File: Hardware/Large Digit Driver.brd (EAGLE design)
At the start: 45.7 x 22.9 mm, 28 parts, among them U1 TPIC6C596

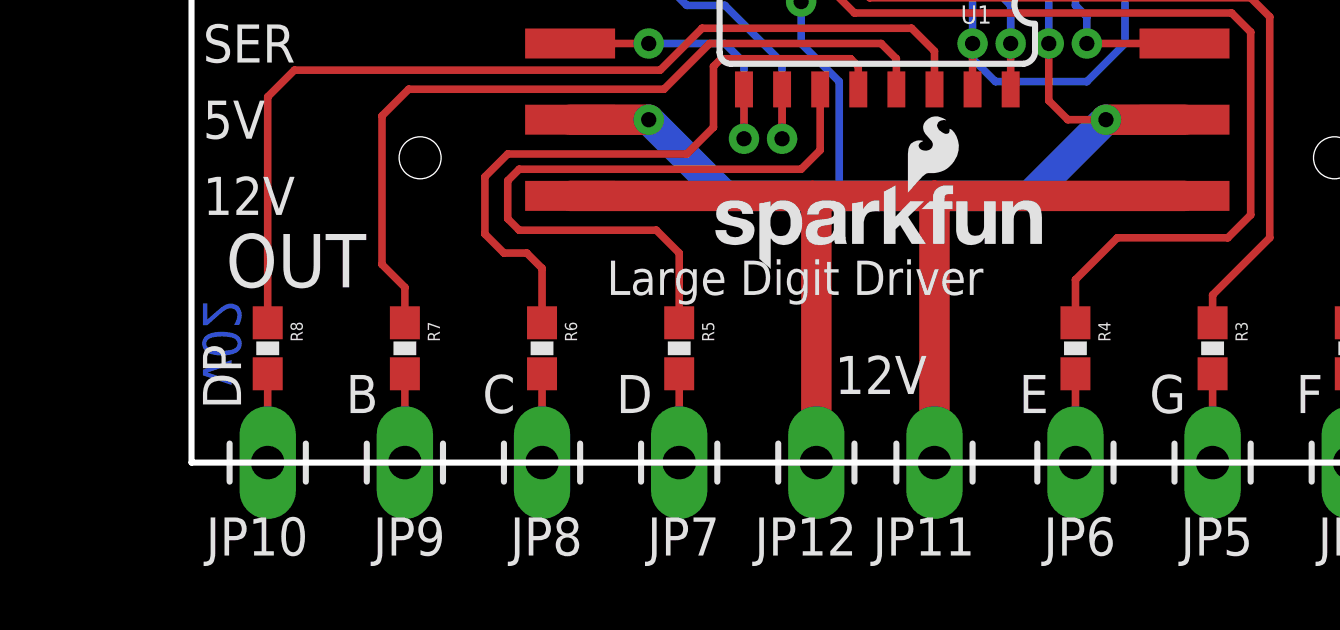
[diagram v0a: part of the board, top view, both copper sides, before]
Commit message: Changing to 15 Ohm limiting resistors. Adding example code.
20 Ohm resistors brought current down to 11mA in testing. Decreasing
resistor size to get higher current per segment.
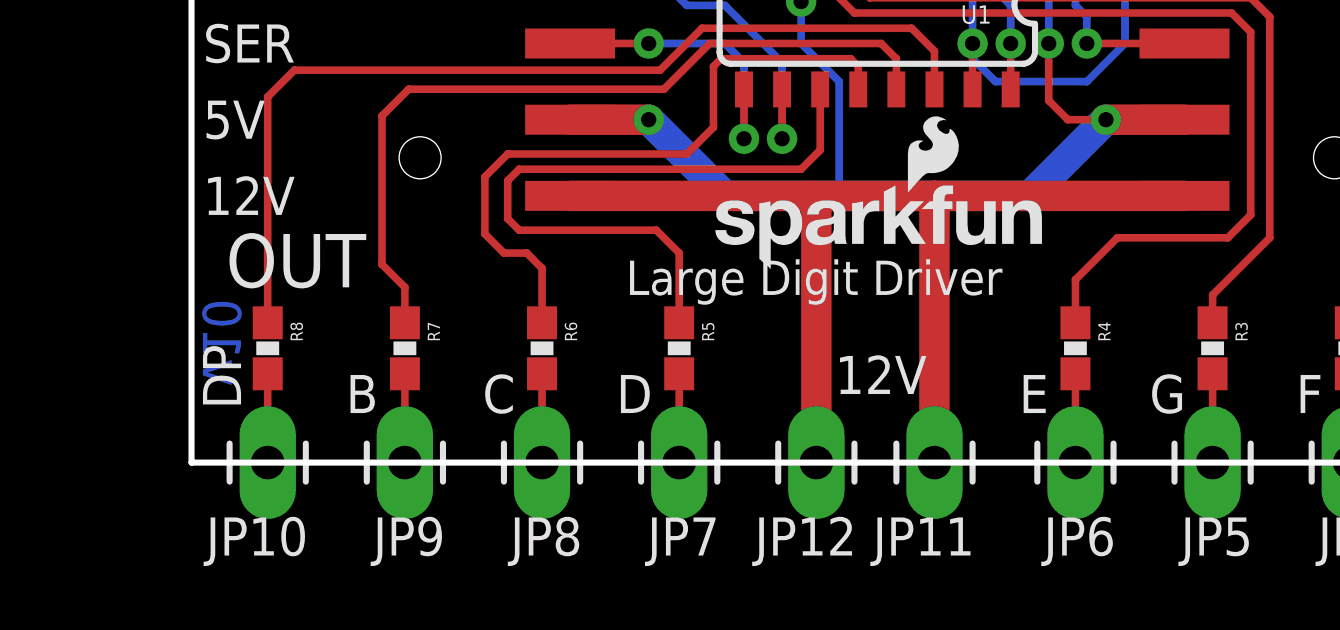
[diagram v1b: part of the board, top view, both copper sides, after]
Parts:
- R1, R2, R3, R4, R5, R6, R7, R8: value 20 -> 15

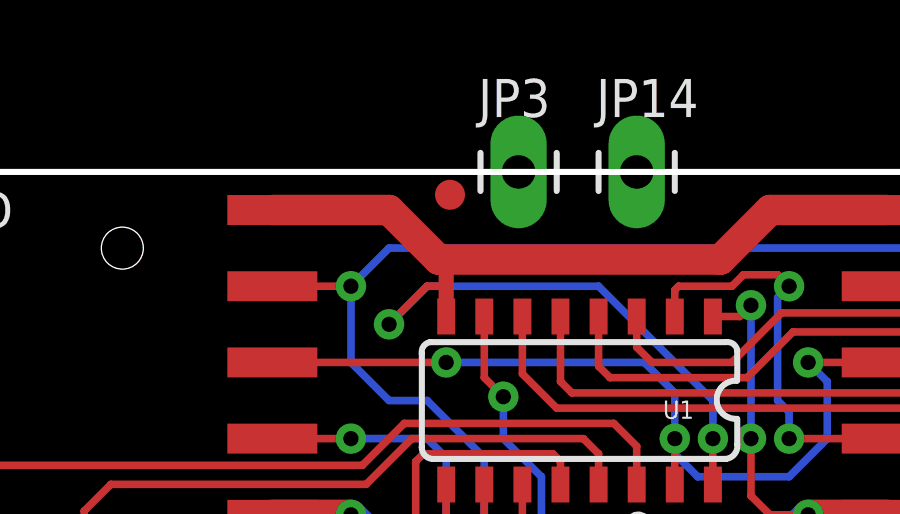
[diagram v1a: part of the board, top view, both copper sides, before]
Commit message: Fiducial bump. Adding silk on bottom.
Fixes issue #3.
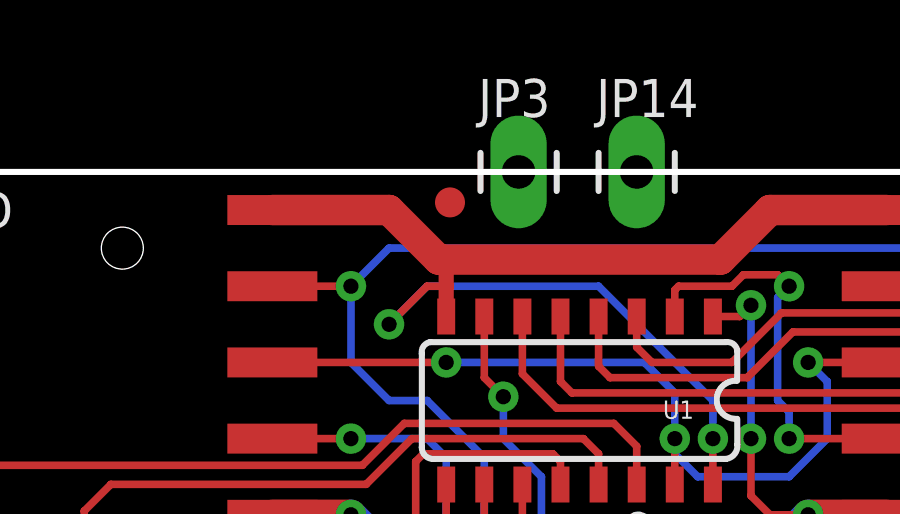
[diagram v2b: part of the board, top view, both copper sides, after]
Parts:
- moved FID1 0.25 mm to (18.5, 21.8)
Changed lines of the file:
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@@
 <?xml version="1.0" encoding="utf-8"?>
 <!DOCTYPE eagle SYSTEM "eagle.dtd">
-<eagle version="7.1.0">
+<eagle version="7.2.0">
 <drawing>
 <settings>
@@
 <layer number="223" name="223bmp" color="24" fill="1" visible="no" active="no"/>
 <layer number="224" name="224bmp" color="25" fill="1" visible="no" active="no"/>
-<layer number="225" name="225bmp" color="7" fill="1" visible="yes" active="yes"/>
-<layer number="226" name="226bmp" color="7" fill="1" visible="yes" active="yes"/>
-<layer number="227" name="227bmp" color="7" fill="1" visible="yes" active="yes"/>
-<layer number="228" name="228bmp" color="7" fill="1" visible="yes" active="yes"/>
-<layer number="229" name="229bmp" color="7" fill="1" visible="yes" active="yes"/>
-<layer number="230" name="230bmp" color="7" fill="1" visible="yes" active="yes"/>
-<layer number="231" name="231bmp" color="7" fill="1" visible="yes" active="yes"/>
+<layer number="225" name="225bmp" color="7" fill="1" visible="no" active="yes"/>
+<layer number="226" name="226bmp" color="7" fill="1" visible="no" active="yes"/>
+<layer number="227" name="227bmp" color="7" fill="1" visible="no" active="yes"/>
+<layer number="228" name="228bmp" color="7" fill="1" visible="no" active="yes"/>
+<layer number="229" name="229bmp" color="7" fill="1" visible="no" active="yes"/>
+<layer number="230" name="230bmp" color="7" fill="1" visible="no" active="yes"/>
+<layer number="231" name="231bmp" color="7" fill="1" visible="no" active="yes"/>
 <layer number="248" name="Housing" color="7" fill="1" visible="no" active="yes"/>
 <layer number="249" name="Edge" color="7" fill="1" visible="no" active="yes"/>
@@
 <dimension x1="0" y1="22.86" x2="6.35" y2="22.86" x3="3.175" y3="25.4" textsize="1.778" textratio="15" layer="47" unit="inch"/>
 <text x="-21.59" y="-8.89" size="1.778" layer="20" font="vector" ratio="15">Leave room on panel for these castelated holes to be milled.</text>
+<text x="5.588" y="5.842" size="1.778" layer="22" font="vector" ratio="15" rot="MR0">OUT</text>
+<text x="43.688" y="5.842" size="1.778" layer="22" font="vector" ratio="15" rot="MR0">IN</text>
 </plain>
 <attributes>
@@
 <element name="JP3" library="SparkFun-Connectors" package="1X01_LONGPAD" value="Anchor" x="20.828" y="22.86"/>
 <element name="JP14" library="SparkFun-Connectors" package="1X01_LONGPAD" value="Anchor" x="24.765" y="22.86"/>
-<element name="FID1" library="SparkFun-Aesthetics" package="FIDUCIAL-1X2" value="FIDUCIAL1X2" x="18.542" y="22.098"/>
+<element name="FID1" library="SparkFun-Aesthetics" package="FIDUCIAL-1X2" value="FIDUCIAL1X2" x="18.542" y="21.844"/>
 <element name="FID2" library="SparkFun-Aesthetics" package="FIDUCIAL-1X2" value="FIDUCIAL1X2" x="44.45" y="3.81"/>
 </elements>

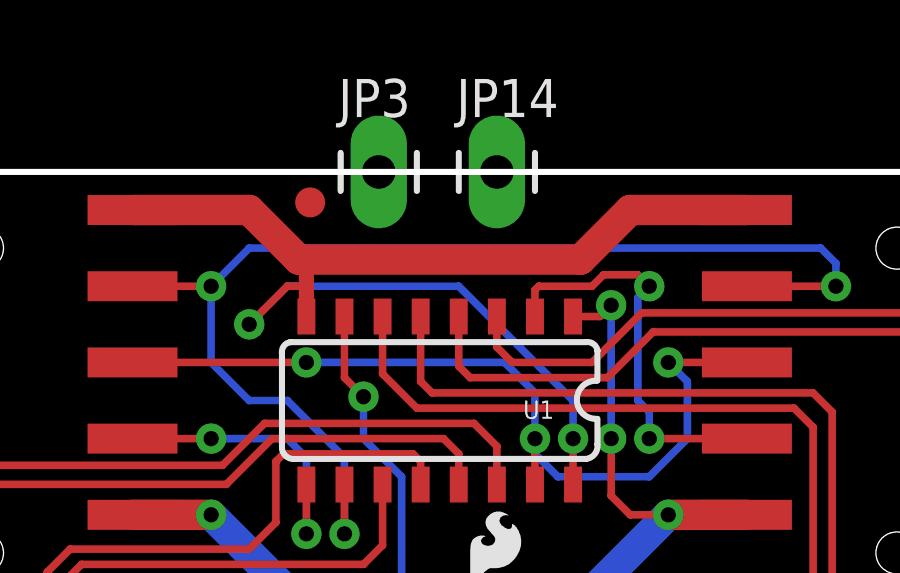
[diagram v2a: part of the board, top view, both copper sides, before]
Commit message: Added silk to anchors. Added power notes to schematic.
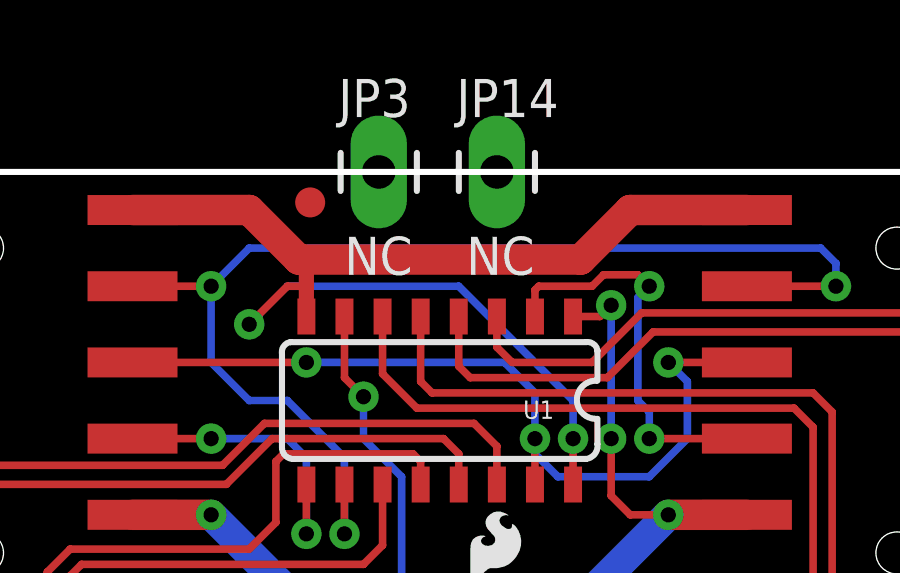
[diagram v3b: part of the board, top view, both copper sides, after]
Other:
- board text added: "NC"
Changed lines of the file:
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@@
 <layer number="47" name="Measures" color="7" fill="1" visible="no" active="yes"/>
 <layer number="48" name="Document" color="7" fill="1" visible="no" active="yes"/>
-<layer number="49" name="Reference" color="11" fill="1" visible="no" active="yes"/>
+<layer number="49" name="Reference" color="11" fill="1" visible="yes" active="yes"/>
 <layer number="50" name="dxf" color="7" fill="1" visible="no" active="no"/>
 <layer number="51" name="tDocu" color="6" fill="1" visible="yes" active="yes"/>
@@
 <text x="5.588" y="5.842" size="1.778" layer="22" font="vector" ratio="15" rot="MR0">OUT</text>
 <text x="43.688" y="5.842" size="1.778" layer="22" font="vector" ratio="15" rot="MR0">IN</text>
+<text x="19.685" y="19.431" size="1.27" layer="21" font="vector" ratio="15">NC</text>
+<text x="23.749" y="19.431" size="1.27" layer="21" font="vector" ratio="15">NC</text>
 </plain>
 <attributes>
